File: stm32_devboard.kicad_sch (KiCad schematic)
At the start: 30 parts, among them SW1 Reset, SW2 User_Press, U1 XC6206P332MR-G, U2 STM32F072CBT6, Y1 8MHz

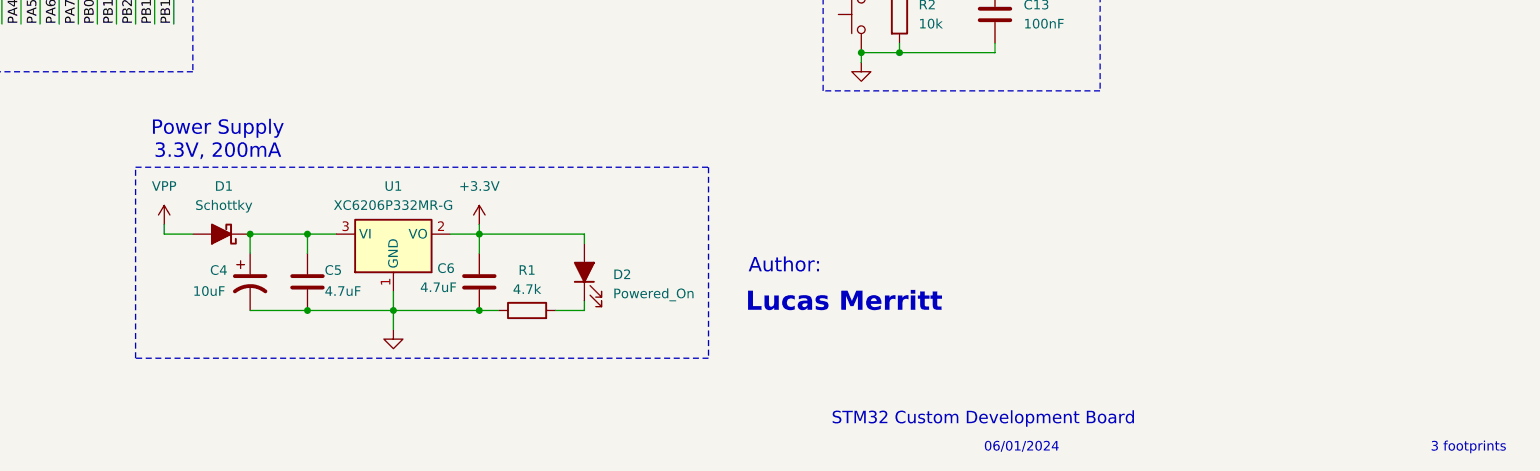
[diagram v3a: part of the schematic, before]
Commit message: Add new footprints
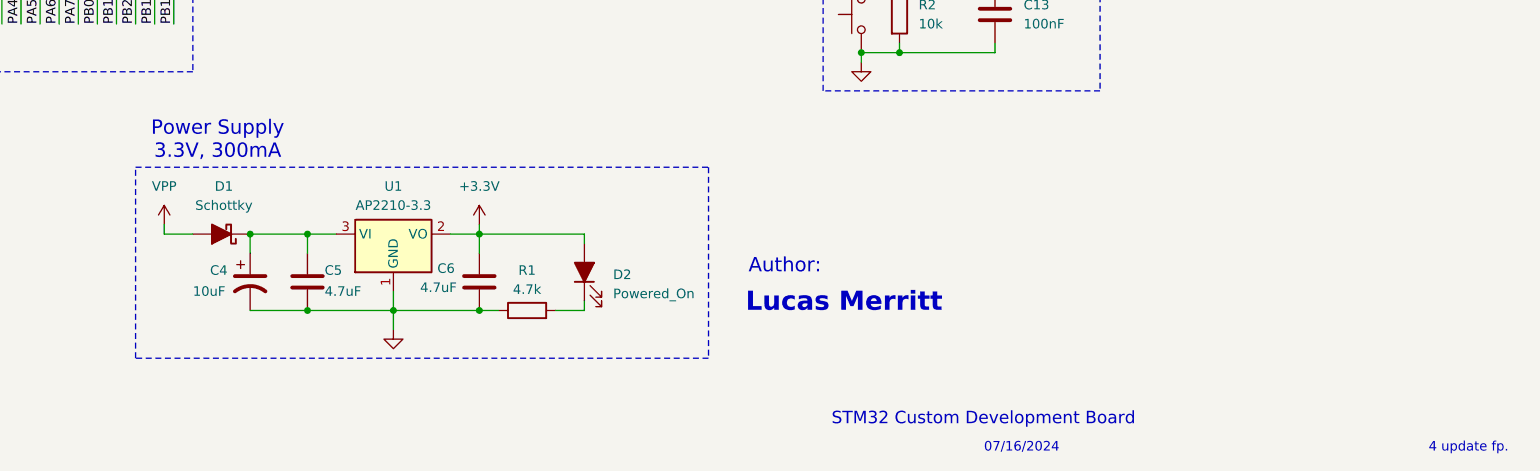
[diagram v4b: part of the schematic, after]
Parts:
- C1, C3: footprint Capacitor_SMD:C_0805_2012Metric -> Capacitor_SMD:C_0805_2012Metric_Pad1.18x1.45mm_HandSolder
- C10, C11, C12, C13, C14, C15, C2, C5, C6, C7, C8, C9: footprint Capacitor_SMD:C_0402_1005Metric -> Capacitor_SMD:C_0805_2012Metric_Pad1.18x1.45mm_HandSolder
- C4: footprint Capacitor_Tantalum_SMD:CP_EIA-3216-18_Kemet-A -> Capacitor_SMD:C_1206_3216Metric_Pad1.33x1.80mm_HandSolder
- D2: footprint LED_SMD:LED_0603_1608Metric -> LED_SMD:LED_0805_2012Metric_Pad1.15x1.40mm_HandSolder
- D3: footprint LED_SMD:LED_0805_2012Metric -> LED_SMD:LED_0805_2012Metric_Pad1.15x1.40mm_HandSolder
- R1, R4: footprint Resistor_SMD:R_0805_2012Metric -> Resistor_SMD:R_0805_2012Metric_Pad1.20x1.40mm_HandSolder
- R2, R3: footprint Resistor_SMD:R_0402_1005Metric -> Resistor_SMD:R_0805_2012Metric_Pad1.20x1.40mm_HandSolder
- U1: value XC6206P332MR-G -> AP2210-3.3
- Y1: footprint Crystal:Crystal_SMD_HC49-SD -> Crystal:Crystal_SMD_3225-4Pin_3.2x2.5mm_HandSoldering
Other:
- note added: "07/16/2024"
- note added: "4 update fp."
- note added: "Power Supply 3.3V, 300mA"
- note removed: "06/01/2024"
- note removed: "3 footprints"
- note removed: "Power Supply 3.3V, 200mA"
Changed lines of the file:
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@@
 		)
 	)
-	(text "06/01/2024\n"
+	(text "07/16/2024\n"
 		(exclude_from_sim no)
 		(at 215.646 193.548 0)
@@
 		)
 	)
-	(text "Power Supply\n3.3V, 200mA"
+	(text "Power Supply\n3.3V, 300mA"
 		(exclude_from_sim no)
 		(at 108.712 152.654 0)
@@
 		)
 	)
-	(text "3 footprints"
+	(text "4 update fp."
 		(exclude_from_sim no)
 		(at 275.082 193.548 0)
@@
 			)
 		)
-		(property "Footprint" "Resistor_SMD:R_0402_1005Metric"
+		(property "Footprint" "Resistor_SMD:R_0805_2012Metric_Pad1.20x1.40mm_HandSolder"
 			(at 197.612 135.89 90)
 			(effects
@@
 			)
 		)
-		(property "Footprint" "Capacitor_SMD:C_0402_1005Metric"
+		(property "Footprint" "Capacitor_SMD:C_0805_2012Metric_Pad1.18x1.45mm_HandSolder"
 			(at 194.0052 45.72 0)
 			(effects
@@
 			)
 		)
-		(property "Footprint" "Capacitor_SMD:C_0402_1005Metric"
+		(property "Footprint" "Capacitor_SMD:C_0805_2012Metric_Pad1.18x1.45mm_HandSolder"
 			(at 205.4352 93.98 0)
 			(effects
@@
 			)
 		)
-		(property "Footprint" "Capacitor_SMD:C_0402_1005Metric"
+		(property "Footprint" "Capacitor_SMD:C_0805_2012Metric_Pad1.18x1.45mm_HandSolder"
 			(at 194.0052 93.98 0)
 			(effects
@@
 			)
 		)
-		(property "Footprint" "Capacitor_SMD:C_0402_1005Metric"
+		(property "Footprint" "Capacitor_SMD:C_0805_2012Metric_Pad1.18x1.45mm_HandSolder"
 			(at 223.2152 45.72 0)
 			(effects
@@
 			)
 		)
-		(property "Footprint" "Resistor_SMD:R_0402_1005Metric"
+		(property "Footprint" "Resistor_SMD:R_0805_2012Metric_Pad1.20x1.40mm_HandSolder"
 			(at 205.74 131.318 90)
 			(effects
@@
 			)
 		)
-		(property "Footprint" "Resistor_SMD:R_0805_2012Metric"
+		(property "Footprint" "Resistor_SMD:R_0805_2012Metric_Pad1.20x1.40mm_HandSolder"
 			(at 218.44 121.158 90)
 			(effects
@@
 			)
 		)
-		(property "Footprint" "Capacitor_SMD:C_0402_1005Metric"
+		(property "Footprint" "Capacitor_SMD:C_0805_2012Metric_Pad1.18x1.45mm_HandSolder"
 			(at 237.1852 45.72 0)
 			(effects
@@
 			)
 		)
-		(property "Footprint" "Resistor_SMD:R_0805_2012Metric"
+		(property "Footprint" "Resistor_SMD:R_0805_2012Metric_Pad1.20x1.40mm_HandSolder"
 			(at 149.86 177.038 90)
 			(effects
@@
 			)
 		)
-		(property "Footprint" "Crystal:Crystal_SMD_HC49-SD"
+		(property "Footprint" "Crystal:Crystal_SMD_3225-4Pin_3.2x2.5mm_HandSoldering"
 			(at 87.63 72.39 0)
 			(effects
@@
 			)
 		)
-		(property "Value" "XC6206P332MR-G"
+		(property "Value" "AP2210-3.3"
 			(at 132.08 161.29 0)
 			(effects
@@
 			)
 		)
-		(property "Footprint" "Capacitor_SMD:C_0402_1005Metric"
+		(property "Footprint" "Capacitor_SMD:C_0805_2012Metric_Pad1.18x1.45mm_HandSolder"
 			(at 213.0552 139.7 0)
 			(effects
@@
 			)
 		)
-		(property "Footprint" "Capacitor_SMD:C_0402_1005Metric"
+		(property "Footprint" "Capacitor_SMD:C_0805_2012Metric_Pad1.18x1.45mm_HandSolder"
 			(at 207.9752 66.04 0)
 			(effects
@@
 			)
 		)
-		(property "Footprint" "Capacitor_SMD:C_0402_1005Metric"
+		(property "Footprint" "Capacitor_SMD:C_0805_2012Metric_Pad1.18x1.45mm_HandSolder"
 			(at 92.4052 45.72 0)
 			(effects
@@
 			)
 		)
-		(property "Footprint" "Capacitor_SMD:C_0402_1005Metric"
+		(property "Footprint" "Capacitor_SMD:C_0805_2012Metric_Pad1.18x1.45mm_HandSolder"
 			(at 144.4752 175.26 0)
 			(effects
@@
 			)
 		)
-		(property "Footprint" "Capacitor_SMD:C_0402_1005Metric"
+		(property "Footprint" "Capacitor_SMD:C_0805_2012Metric_Pad1.18x1.45mm_HandSolder"
 			(at 207.9752 45.72 0)
 			(effects
@@
 			)
 		)
-		(property "Footprint" "LED_SMD:LED_0805_2012Metric"
+		(property "Footprint" "LED_SMD:LED_0805_2012Metric_Pad1.15x1.40mm_HandSolder"
 			(at 205.74 119.38 0)
 			(effects
@@
 			)
 		)
-		(property "Footprint" "Capacitor_SMD:C_0805_2012Metric"
+		(property "Footprint" "Capacitor_SMD:C_0805_2012Metric_Pad1.18x1.45mm_HandSolder"
 			(at 94.9452 82.55 0)
 			(effects
@@
 			)
 		)
-		(property "Footprint" "Capacitor_SMD:C_0402_1005Metric"
+		(property "Footprint" "Capacitor_SMD:C_0805_2012Metric_Pad1.18x1.45mm_HandSolder"
 			(at 121.6152 175.26 0)
 			(effects
@@
 			)
 		)
-		(property "Footprint" "Capacitor_Tantalum_SMD:CP_EIA-3216-18_Kemet-A"
+		(property "Footprint" "Capacitor_SMD:C_1206_3216Metric_Pad1.33x1.80mm_HandSolder"
 			(at 113.03 171.45 0)
 			(effects
@@
 			)
 		)
-		(property "Footprint" "LED_SMD:LED_0603_1608Metric"
+		(property "Footprint" "LED_SMD:LED_0805_2012Metric_Pad1.15x1.40mm_HandSolder"
 			(at 157.48 170.18 0)
 			(effects
@@
 			)
 		)
-		(property "Footprint" "Capacitor_SMD:C_0402_1005Metric"
+		(property "Footprint" "Capacitor_SMD:C_0805_2012Metric_Pad1.18x1.45mm_HandSolder"
 			(at 194.0052 66.04 0)
 			(effects
@@
 			)
 		)
-		(property "Footprint" "Capacitor_SMD:C_0805_2012Metric"
+		(property "Footprint" "Capacitor_SMD:C_0805_2012Metric_Pad1.18x1.45mm_HandSolder"
 			(at 82.2452 82.55 0)
 			(effects

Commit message: update schem
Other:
- note removed: "07/16/2024"
- note removed: "4 update fp."
- note removed: "STM32 Custom Development Board"
- title: (none) -> STM32 Custom Development Board
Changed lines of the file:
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@@
 	(generator_version "8.0")
 	(paper "A4")
+	(title_block
+		(title "STM32 Custom Development Board")
+		(date "2024-07-27")
+		(rev "4 update fp.")
+	)
 	(junction
 		(at 142.24 123.19)
@@
 			)
 			(justify left)
-		)
-	)
-	(text "07/16/2024\n"
-		(exclude_from_sim no)
-		(at 215.646 193.548 0)
-		(effects
-			(font
-				(size 1.27 1.27)
-				(color 132 0 0 1)
-			)
 		)
 	)
@@
 		)
 	)
-	(text "STM32 Custom Development Board"
-		(exclude_from_sim no)
-		(at 210.566 189.738 0)
-		(effects
-			(font
-				(size 1.651 1.651)
-				(color 132 0 0 1)
-			)
-		)
-	)
 	(text "Pin has internal \nfiltering"
 		(exclude_from_sim no)
@@
 			)
 		)
-	)
-	(text "4 update fp."
-		(exclude_from_sim no)
-		(at 275.082 193.548 0)
-		(effects
-			(font
-				(size 1.27 1.27)
-				(color 132 0 0 1)
-			)
-		)

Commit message: rev1
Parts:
- Y1: footprint Crystal:Crystal_SMD_3225-4Pin_3.2x2.5mm_HandSoldering -> Crystal:Crystal_SMD_Abracon_ABM3-2Pin_5.0x3.2mm_HandSoldering
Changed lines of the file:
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@@
 			)
 		)
-		(property "Footprint" "Crystal:Crystal_SMD_3225-4Pin_3.2x2.5mm_HandSoldering"
+		(property "Footprint" "Crystal:Crystal_SMD_Abracon_ABM3-2Pin_5.0x3.2mm_HandSoldering"
 			(at 87.63 72.39 0)
 			(effects
